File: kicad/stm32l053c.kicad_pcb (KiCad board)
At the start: 2 copper layers, 26.7 x 43.2 mm, 45 parts, among them J1 GND, J10 3V3, J11 I2C, J2 GND, J3 TX, J4 GND, J5 TEST_1P, J6 TEST_1P, J8 RX, P1 SWD, U1 AP2112, U2 STM32L053C8_LQFP48, U3 ADS1015, U4 UFL_SMA, U5 RFM92/95

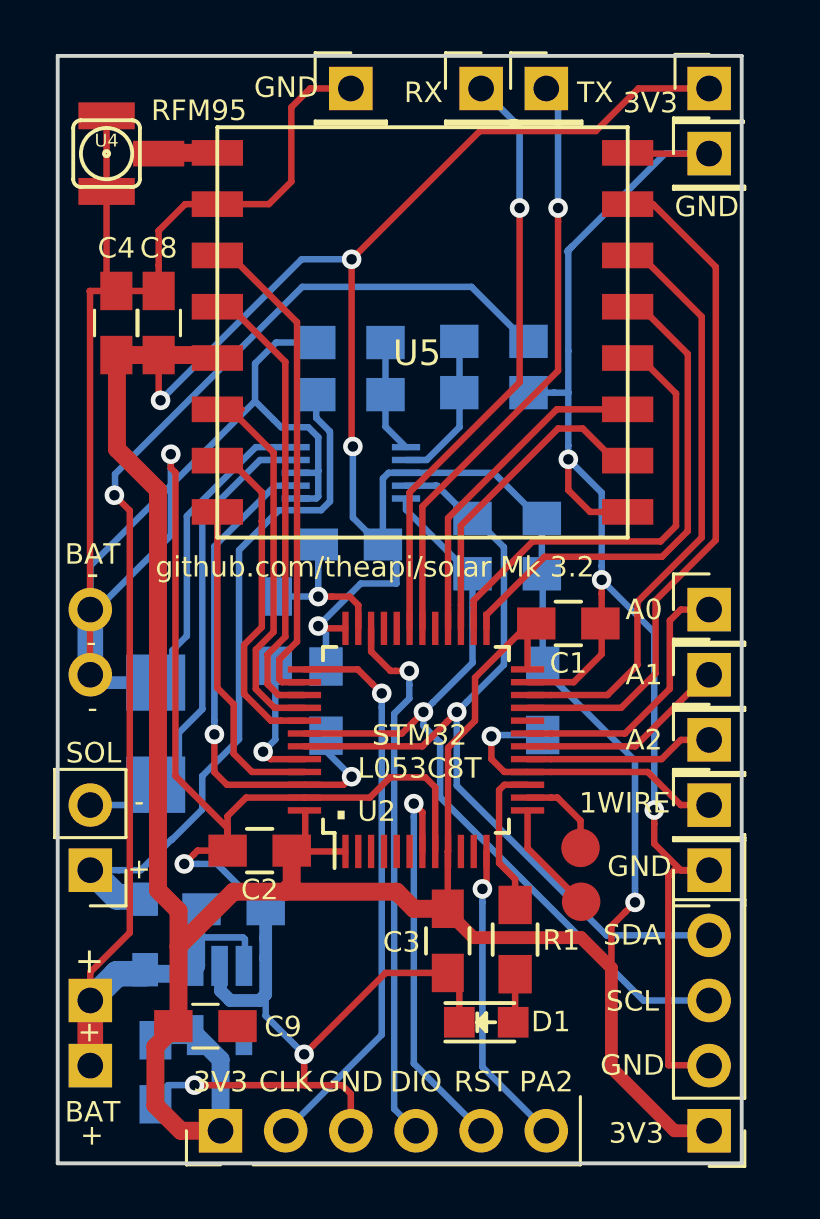
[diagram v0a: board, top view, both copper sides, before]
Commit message: External voltage regulator & shunt
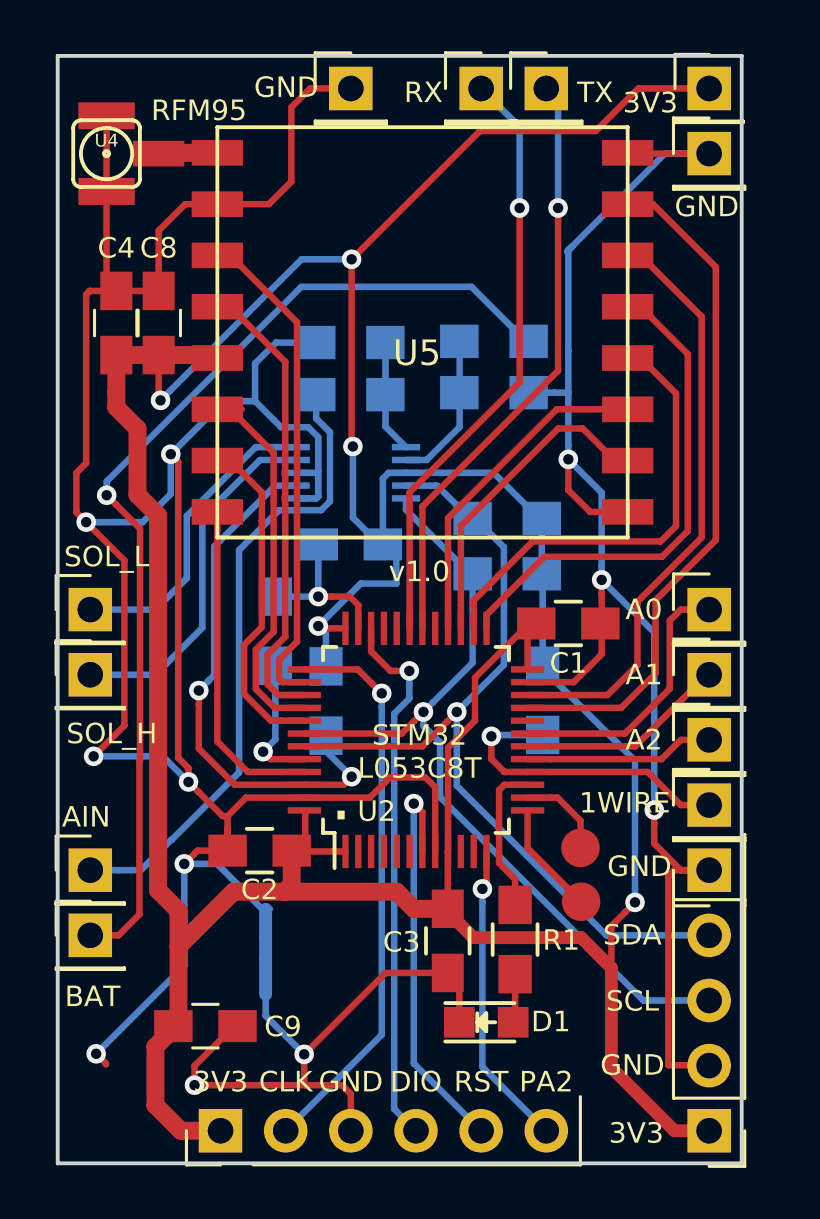
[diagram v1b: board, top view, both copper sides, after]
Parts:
- removed BT1: Battery, theapi:BatteryBoxAndPins
- removed C5, C6: 1uf, Capacitors_SMD:C_0805_HandSoldering
- removed D2: D_Schottky, theapi:D_SOD-323_HandSoldering
- removed R5: R_Shunt, theapi:SHUNT_1210_HandSoldering
- removed REF**: TheApiLogoTiny, theapi:TheApiLogoTiny
- removed REF**: TheApiLogo, theapi:TheApiLogoSmall
- removed SC1: Solar_Cells, Pin_Headers:Pin_Header_Straight_1x02_Pitch2.54mm
- removed U1: AP2112, TO_SOT_Packages_SMD:SOT-23-5_HandSoldering
- added J12: AIN, Pin_Headers:Pin_Header_Straight_1x01_Pitch2.54mm, F.Cu at (137.2, 83.8)
- added J13: SOL_SENSE_L, Pin_Headers:Pin_Header_Straight_1x01_Pitch2.54mm, F.Cu at (137.2, 73.7)
- added J7: BATT_SENSE, Pin_Headers:Pin_Header_Straight_1x01_Pitch2.54mm, F.Cu at (137.2, 86.4)
- added J9: SOL_SENSE_H, Pin_Headers:Pin_Header_Straight_1x01_Pitch2.54mm, F.Cu at (137.2, 76.2)
- C1, C2, C3: value 100nF -> 0.1uF
- C7: value 10uF -> 0.1uF
- R6: value 300K -> 620K
- R8: value 100K -> 620K
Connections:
- net /PA3 renamed /USART2_RX
- net PA2 renamed USART2_TX
- R6 pad 1: Net-(D2-Pad2) -> /AIN
- U2 pad 10: Net-(U2-Pad10) -> (no net)
- U2 pad 11: Net-(U2-Pad11) -> (no net)
- U2 pad 2: Net-(U2-Pad2) -> (no net)
- U2 pad 20: Net-(U2-Pad20) -> (no net)
- U2 pad 29: Net-(U2-Pad29) -> (no net)
- U2 pad 3: Net-(U2-Pad3) -> (no net)
- U2 pad 32: Net-(U2-Pad32) -> (no net)
- U2 pad 33: Net-(U2-Pad33) -> (no net)
- U2 pad 4: Net-(U2-Pad4) -> (no net)
- U2 pad 5: Net-(U2-Pad5) -> (no net)
- U2 pad 6: Net-(U2-Pad6) -> (no net)
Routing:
- net Net-(D2-Pad2): track 27.4 -> 0.00 mm
- net /AIN: track 0.00 -> 24.8 mm
- net /BATT: track 54.0 -> 40.2 mm
- net +3V3: track 172.7 -> 167.0 mm
- net Net-(R5-Pad1): track 2.47 -> 0.00 mm
- net /AIN0: track 15.4 -> 14.0 mm
- net Earth: track 210.2 -> 209.7 mm, vias 8 -> 12
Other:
- board text added: "AIN"
- board text added: "SOL_H"
- board text added: "SOL_L"
- board text added: "github.com/theapi/ gard_comms_hardware v1.0"
- board text added: "v1.0"
- board text removed: "+"
- board text removed: "-"
- board text removed: "SOL"
- board text removed: "github.com/theapi/solar Mk 3.2"
